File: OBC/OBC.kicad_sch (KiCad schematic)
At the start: 9 parts, among them J2 IDC1 (PMS-Raspi), J3 IDC2 (Raspi-TRU), J5 Conn_01x04, J6 Modo de operación, U1 MPU9250, U2 BMP280, U3 RASPBERRY_PI_ZERO_2_W

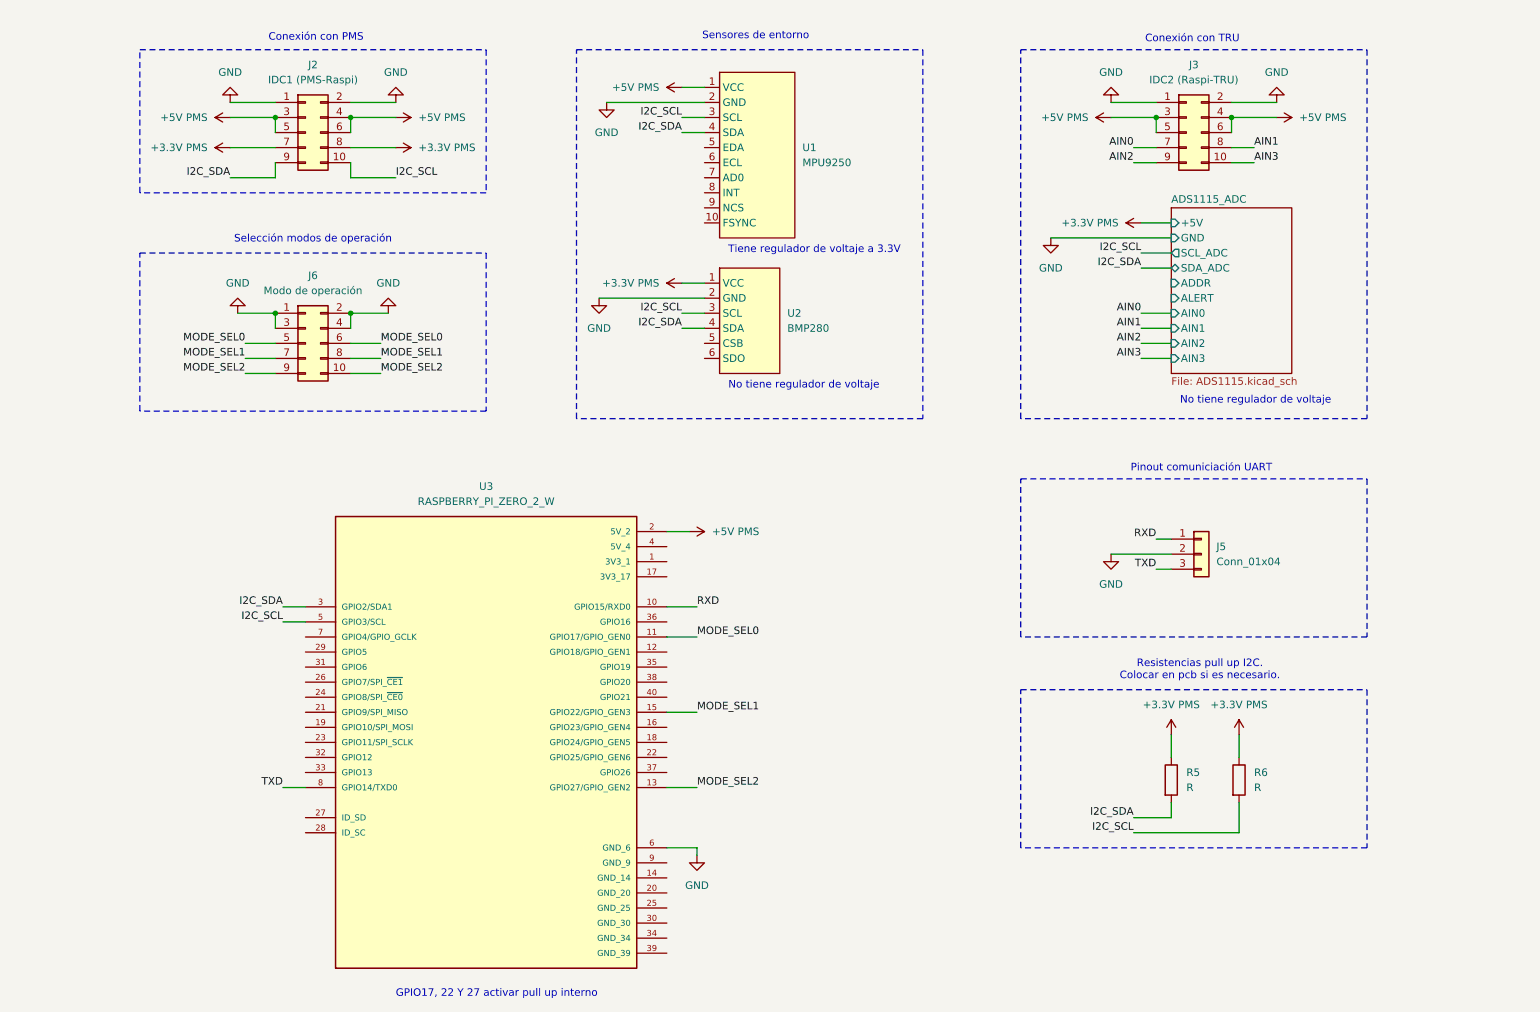
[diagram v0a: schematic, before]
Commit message: Conecta pines int a gpio
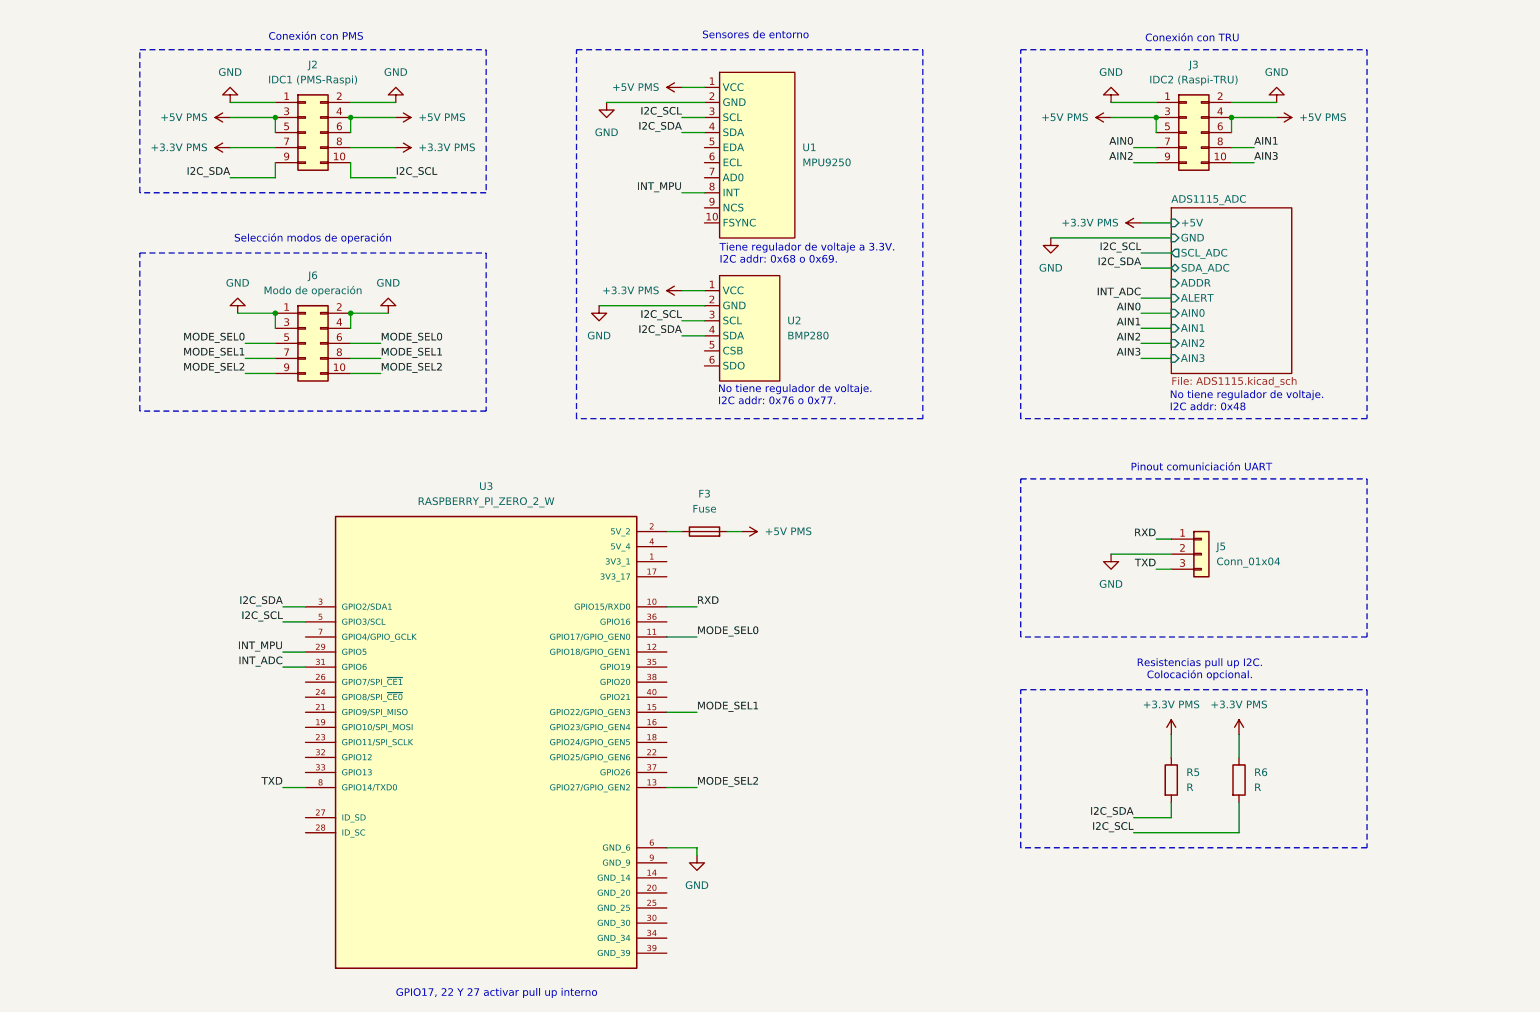
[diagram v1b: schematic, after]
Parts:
- added F3: Fuse, symbol Device:Fuse
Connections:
- net +5V PMS: now also F3.2; no longer U3.2 (5V_2)
- net INT_MPU: now reaches U1.8 (INT)
- net INT_MPU: now also U3.29 (GPIO5)
- net INT_ADC: now reaches U3.31 (GPIO6)
- new net: F3.1, U3.2 (5V_2)
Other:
- note added: "No tiene regulador de voltaje. I2C addr: 0x48"
- note added: "No tiene regulador de voltaje. I2C addr: 0x76 o 0x77."
- note added: "Resistencias pull up I2C. Colocación opcional."
- note added: "Tiene regulador de voltaje a 3.3V. I2C addr: 0x68 o 0x69."
- note removed: "No tiene regulador de voltaje"
- note removed: "Resistencias pull up I2C. Colocar en pcb si es necesario."
- note removed: "Tiene regulador de voltaje a 3.3V"
- moved on the sheet: U2

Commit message: Agrega no connect flags
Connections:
- no-connect marks 0 -> 37
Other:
- note added: "No tiene regulador de voltaje. I2C addr: 0x48."
- note removed: "No tiene regulador de voltaje. I2C addr: 0x48"
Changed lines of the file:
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@@
 		)
 	)
-	(text "No tiene regulador de voltaje.\nI2C addr: 0x48"
+	(text "No tiene regulador de voltaje.\nI2C addr: 0x48."
 		(exclude_from_sim no)
 		(at 215.646 86.106 0)
@@
 		(color 0 0 0 0)
 	)
+	(no_connect
+		(at 130.81 113.03)
+	)
+	(no_connect
+		(at 130.81 148.59)
+	)
+	(no_connect
+		(at 130.81 173.99)
+	)
+	(no_connect
+		(at 130.81 140.97)
+	)
+	(no_connect
+		(at 137.16 55.88)
+	)
+	(no_connect
+		(at 130.81 133.35)
+	)
+	(no_connect
+		(at 130.81 166.37)
+	)
+	(no_connect
+		(at 137.16 77.47)
+	)
+	(no_connect
+		(at 69.85 158.75)
+	)
+	(no_connect
+		(at 69.85 148.59)
+	)
+	(no_connect
+		(at 130.81 179.07)
+	)
+	(no_connect
+		(at 69.85 156.21)
+	)
+	(no_connect
+		(at 137.16 43.18)
+	)
+	(no_connect
+		(at 130.81 130.81)
+	)
+	(no_connect
+		(at 69.85 125.73)
+	)
+	(no_connect
+		(at 130.81 163.83)
+	)
+	(no_connect
+		(at 130.81 128.27)
+	)
+	(no_connect
+		(at 130.81 143.51)
+	)
+	(no_connect
+		(at 130.81 171.45)
+	)
+	(no_connect
+		(at 137.16 53.34)
+	)
+	(no_connect
+		(at 130.81 168.91)
+	)
+	(no_connect
+		(at 130.81 135.89)
+	)
+	(no_connect
+		(at 69.85 140.97)
+	)
+	(no_connect
+		(at 69.85 146.05)
+	)
+	(no_connect
+		(at 137.16 45.72)
+	)
+	(no_connect
+		(at 137.16 48.26)
+	)
+	(no_connect
+		(at 130.81 123.19)
+	)
+	(no_connect
+		(at 137.16 80.01)
+	)
+	(no_connect
+		(at 215.9 66.04)
+	)
+	(no_connect
+		(at 130.81 115.57)
+	)
+	(no_connect
+		(at 130.81 110.49)
+	)
+	(no_connect
+		(at 130.81 146.05)
+	)
+	(no_connect
+		(at 69.85 133.35)
+	)
+	(no_connect
+		(at 130.81 176.53)
+	)
+	(no_connect
+		(at 69.85 143.51)
+	)
+	(no_connect
+		(at 69.85 135.89)
+	)
+	(no_connect
+		(at 69.85 138.43)
+	)
 	(wire
